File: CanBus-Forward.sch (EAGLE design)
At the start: 1 part

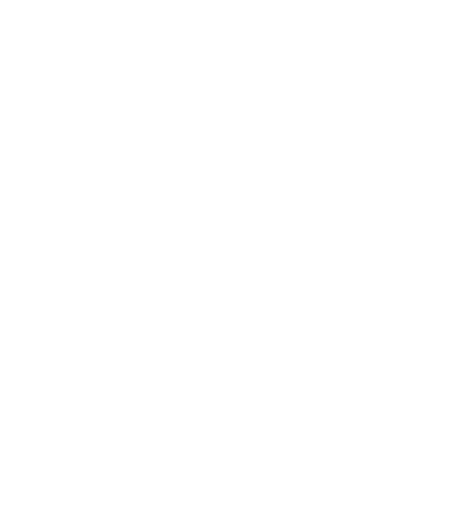
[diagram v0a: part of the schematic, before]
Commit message: CAN-Bus Beadboard-Adapter, Layouts angepasst
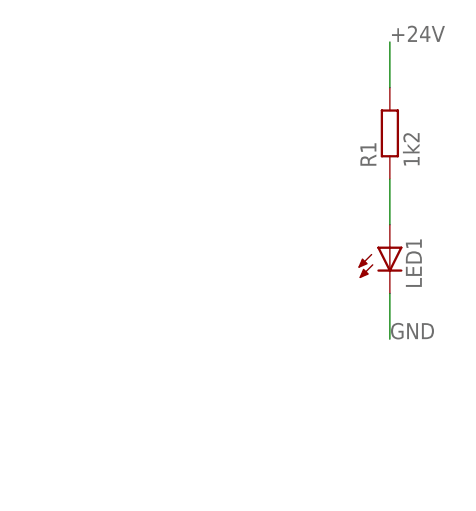
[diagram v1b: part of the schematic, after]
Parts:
- added LED1: (no value), led:LEDCHIPLED_1206
- added R1: 1k2, rcl:R-EU_R1206
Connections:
- new net N$2: LED1.A, R1.1
- net +24V: now also R1.2
- net GND: now also LED1.C
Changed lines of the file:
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@@
 <part name="J1" library="mebp_8-8g" deviceset="555141-1" device=""/>
 <part name="FRAME1" library="frames" deviceset="A4L-LOC" device=""/>
+<part name="LED1" library="led" deviceset="LED" device="CHIPLED_1206"/>
+<part name="R1" library="rcl" deviceset="R-EU_" device="R1206" value="1k2"/>
 </parts>
 <sheets>
@@
 <instance part="J1" gate="G$1" x="43.18" y="55.88"/>
 <instance part="FRAME1" gate="G$1" x="-5.08" y="-5.08"/>
+<instance part="LED1" gate="G$1" x="121.92" y="101.6"/>
+<instance part="R1" gate="G$1" x="121.92" y="114.3" rot="R90"/>
 </instances>
 <busses>
@@
 <label x="50.8" y="43.18" size="1.778" layer="95"/>
 </segment>
+<segment>
+<pinref part="LED1" gate="G$1" pin="C"/>
+<wire x1="121.92" y1="96.52" x2="121.92" y2="91.44" width="0.1524" layer="91"/>
+<label x="121.92" y="91.44" size="1.778" layer="95"/>
+</segment>
 </net>
 <net name="+24V" class="0">
@@
 <label x="35.56" y="55.88" size="1.778" layer="95" rot="MR0"/>
 </segment>
+<segment>
+<pinref part="R1" gate="G$1" pin="2"/>
+<wire x1="121.92" y1="119.38" x2="121.92" y2="124.46" width="0.1524" layer="91"/>
+<label x="121.92" y="124.46" size="1.778" layer="95"/>
+</segment>
 </net>
+<net name="N$2" class="0">
+<segment>
+<pinref part="R1" gate="G$1" pin="1"/>
+<pinref part="LED1" gate="G$1" pin="A"/>
+<wire x1="121.92" y1="109.22" x2="121.92" y2="104.14" width="0.1524" layer="91"/>
+</segment>
+</net>
